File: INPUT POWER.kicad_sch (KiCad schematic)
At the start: 22 parts, among them J1 TYPE-C-31-M12_13, SW3 ON/OFF, U3 IP5306

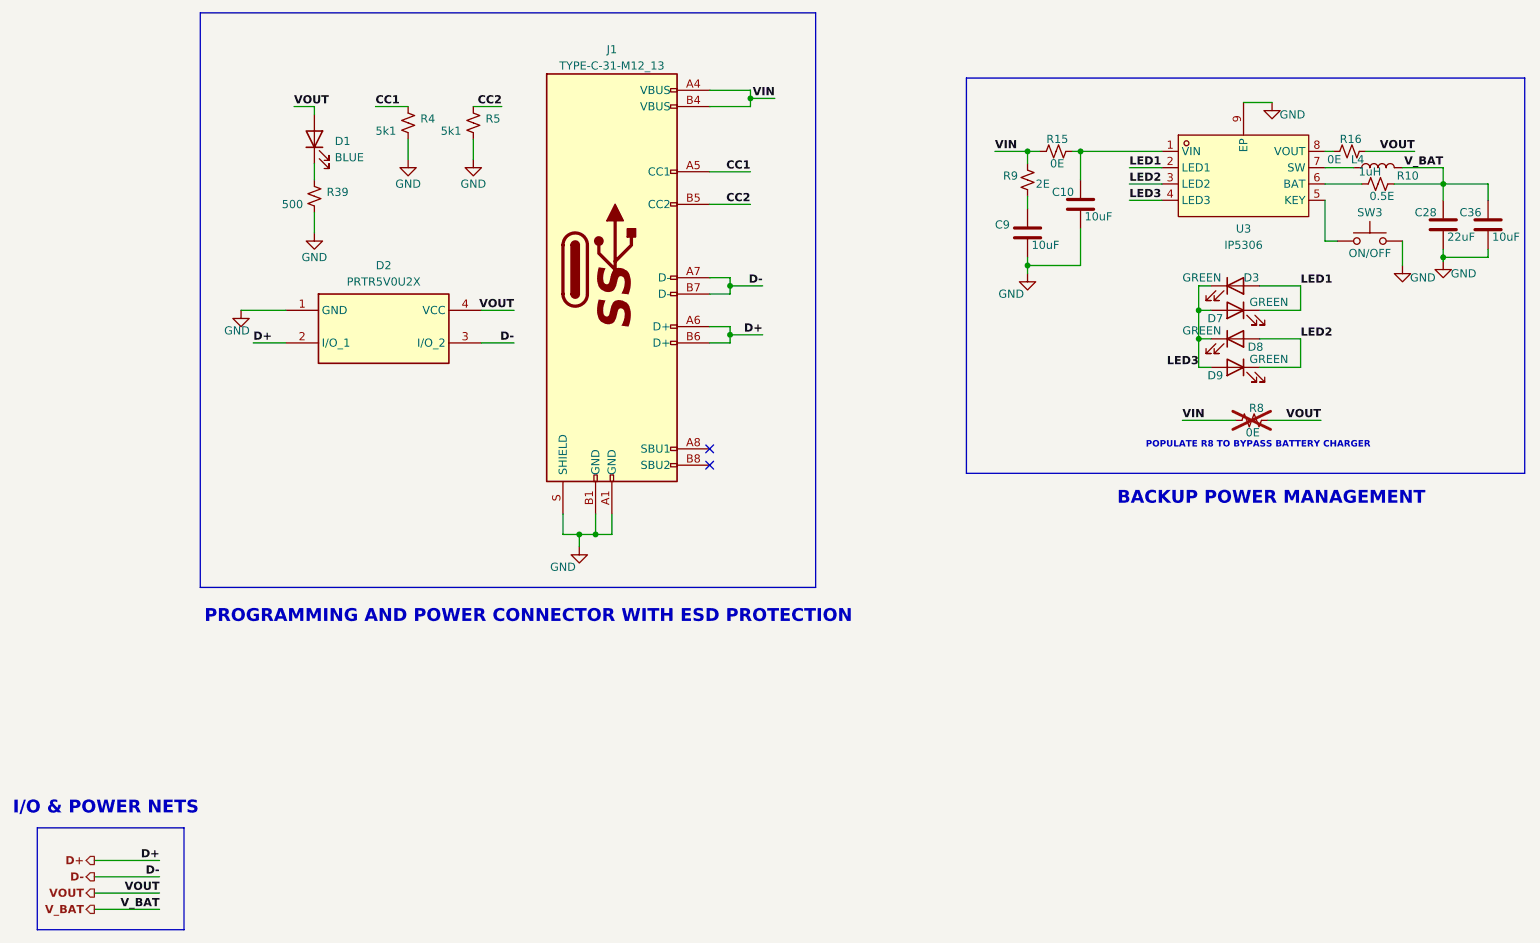
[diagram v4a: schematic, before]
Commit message: Added bulk Decoupling and arranged components
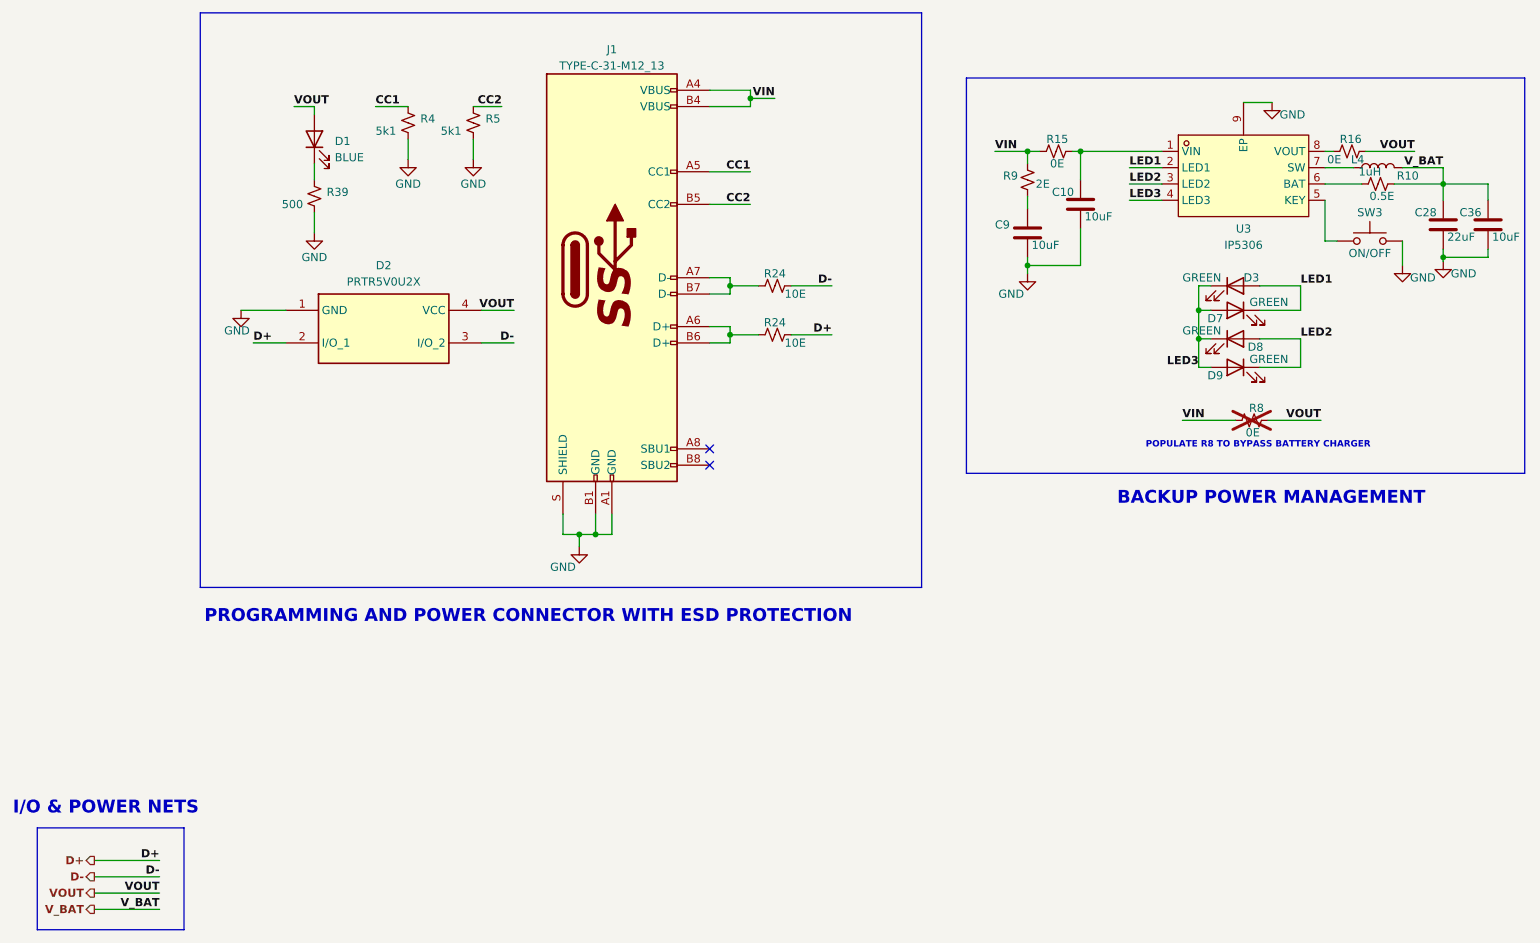
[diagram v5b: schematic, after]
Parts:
- added R24 (x2): 10E, ESP32-S3_Dev_Board:R_0402_1005Metric, symbol ESP32-S3_DB:R_Small_US
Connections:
- net D+: now also R24.2; no longer J1.A6 (D+), J1.B6 (D+)
- net D-: now also R24.2; no longer J1.A7 (D-), J1.B7 (D-)
- new net: J1.A7 (D-), J1.B7 (D-), R24.1
- new net: J1.A6 (D+), J1.B6 (D+), R24.1
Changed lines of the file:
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@@
     (stroke (width 1) (type default) (color 72 72 72 1))
   )
-  (bus (pts (xy 140.97 135.255) (xy 45.085 135.255))
+  (bus (pts (xy 157.48 135.255) (xy 45.085 135.255))
     (stroke (width 1) (type default) (color 72 72 72 1))
   )
@@
     (stroke (width 0) (type default))
   )
-  (wire (pts (xy 132.715 88.265) (xy 127.635 88.265))
+  (wire (pts (xy 143.51 88.265) (xy 137.16 88.265))
     (stroke (width 0) (type default))
   )
@@
     (stroke (width 0) (type default))
   )
-  (bus (pts (xy 45.085 45.72) (xy 140.97 45.72))
-    (stroke (width 1) (type default) (color 72 72 72 1))
-  )
-  (bus (pts (xy 140.97 45.72) (xy 140.97 135.255))
+  (bus (pts (xy 45.085 45.72) (xy 157.48 45.72))
+    (stroke (width 1) (type default) (color 72 72 72 1))
+  )
+  (bus (pts (xy 157.48 45.72) (xy 157.48 135.255))
     (stroke (width 1) (type default) (color 72 72 72 1))
   )
@@
     (stroke (width 0) (type default))
   )
+  (wire (pts (xy 132.08 95.885) (xy 127.635 95.885))
+    (stroke (width 0) (type default))
+  )
   (wire (pts (xy 231.14 72.39) (xy 238.76 72.39))
     (stroke (width 0) (type default))
@@
     (stroke (width 0) (type default))
   )
-  (wire (pts (xy 132.715 95.885) (xy 127.635 95.885))
+  (wire (pts (xy 143.51 95.885) (xy 137.16 95.885))
     (stroke (width 0) (type default))
   )
@@
   (bus (pts (xy 19.685 172.72) (xy 42.545 172.72))
     (stroke (width 1) (type default) (color 72 72 72 1))
+  )
+  (wire (pts (xy 132.08 88.265) (xy 127.635 88.265))
+    (stroke (width 0) (type default))
   )
   (wire (pts (xy 173.99 85.09) (xy 173.99 83.82))
@@
     (effects (font (size 1.27 1.27) (thickness 0.254) bold (color 255 153 0 1)) (justify left bottom))
   )
-  (label "D-" (at 132.715 88.265 180) (fields_autoplaced)
+  (label "D-" (at 143.51 88.265 180) (fields_autoplaced)
     (effects (font (size 1.27 1.27) (thickness 0.254) bold (color 0 0 255 1)) (justify right bottom))
   )
@@
     (effects (font (size 1.27 1.27) bold (color 132 132 0 1)) (justify right bottom))
   )
-  (label "D+" (at 132.715 95.885 180) (fields_autoplaced)
+  (label "D+" (at 143.51 95.885 180) (fields_autoplaced)
     (effects (font (size 1.27 1.27) (thickness 0.254) bold (color 0 0 255 1)) (justify right bottom))
   )
@@
         )
       )
+    )
+  )
+  (symbol (lib_id "ESP32-S3_DB:R_Small_US") (at 134.62 88.265 90) (unit 1)
+    (in_bom yes) (on_board yes) (dnp no)
+    (property "Reference" "R24" (at 134.62 86.36 90)
+      (effects (font (size 1.27 1.27)))
+    )
+    (property "Value" "10E" (at 137.795 89.535 90)
+      (effects (font (size 1.27 1.27)))
+    )
+    (property "Footprint" "ESP32-S3_Dev_Board:R_0402_1005Metric" (at 134.62 88.265 0)
+      (effects (font (size 1.27 1.27)) hide)
+    )
+    (property "Datasheet" "~" (at 134.62 88.265 0)
+      (effects (font (size 1.27 1.27)) hide)
+    )
+    (property "PN" "RTT02100JTH" (at 134.62 88.265 0)
+      (effects (font (size 1.27 1.27)) hide)
+    )
+    (pin "1")
+    (pin "2")
+    (instances
+      (project "ESP32-S3_DB"
+        (path "/b7fc4bd3-c219-4455-832b-8d795385dcf1/9b4afe2f-79e5-4a56-98d7-d16b193c0e70"
+          (reference "R24") (unit 1)
+        )
+        (path "/b7fc4bd3-c219-4455-832b-8d795385dcf1/95090a63-7b3c-4ea0-92b8-aeafe05264cd"
+          (reference "R47") (unit 1)
+        )
+      )
+    )
+  )
+  (symbol (lib_id "ESP32-S3_DB:R_Small_US") (at 134.62 95.885 90) (unit 1)
+    (in_bom yes) (on_board yes) (dnp no)
+    (property "Reference" "R24" (at 134.62 93.98 90)
+      (effects (font (size 1.27 1.27)))
+    )
+    (property "Value" "10E" (at 137.795 97.155 90)
+      (effects (font (size 1.27 1.27)))
+    )
+    (property "Footprint" "ESP32-S3_Dev_Board:R_0402_1005Metric" (at 134.62 95.885 0)
+      (effects (font (size 1.27 1.27)) hide)
+    )
+    (property "Datasheet" "~" (at 134.62 95.885 0)
+      (effects (font (size 1.27 1.27)) hide)
+    )
+    (property "PN" "RTT02100JTH" (at 134.62 95.885 0)
+      (effects (font (size 1.27 1.27)) hide)
+    )
+    (pin "1")
+    (pin "2")
+    (instances
+      (project "ESP32-S3_DB"
+        (path "/b7fc4bd3-c219-4455-832b-8d795385dcf1/9b4afe2f-79e5-4a56-98d7-d16b193c0e70"
+          (reference "R24") (unit 1)
+        )
+        (path "/b7fc4bd3-c219-4455-832b-8d795385dcf1/95090a63-7b3c-4ea0-92b8-aeafe05264cd"
+          (reference "R48") (unit 1)
+        )
+      )

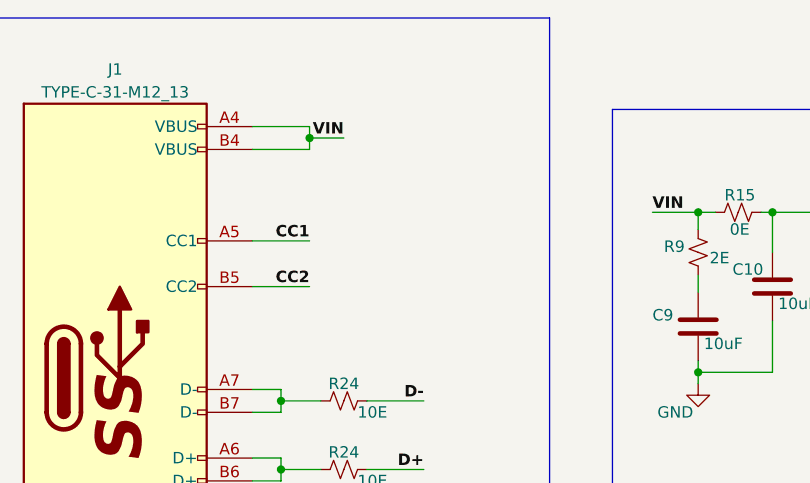
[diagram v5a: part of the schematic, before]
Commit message: Changed USB C footprint and arranged components
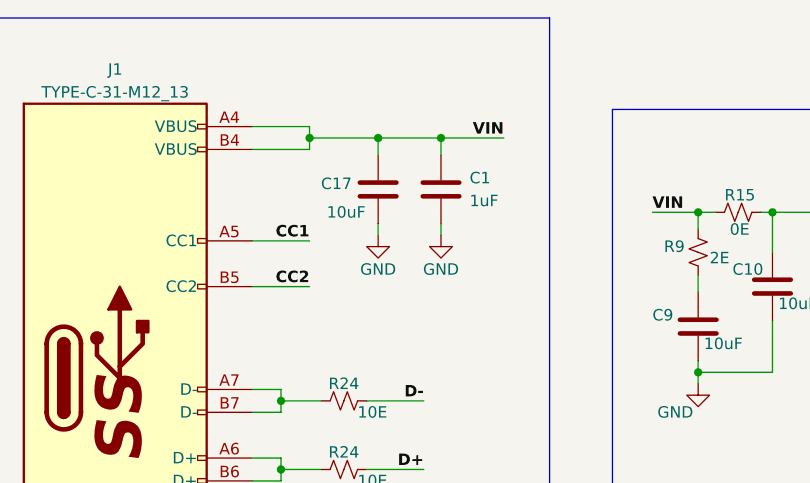
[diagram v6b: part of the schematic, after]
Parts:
- added C1: 1uF, ESP32-S3_Dev_Board:C_0603_1608Metric, symbol ESP32-S3_DB:C
- added C17: 10uF, ESP32-S3_Dev_Board:C_0805_2012Metric, symbol ESP32-S3_DB:C
- J1: footprint ESP32-S3_Dev_Board:USB-C_SMD-TYPE-C-31-M-12 -> ESP32-S3_Dev_Board:tyye_c_connector
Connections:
- net GND: now also C1.2, C17.2
- net VIN: now also C1.1, C17.1
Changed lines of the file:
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@@
 (kicad_sch (version 20230121) (generator eeschema)
   (paper "A4")
+  (junction (at 138.43 59.055) (diameter 0) (color 0 0 0 0)
+  )
   (junction (at 106.68 127) (diameter 0) (color 0 0 0 0)
   )
@@
   )
   (junction (at 238.76 83.82) (diameter 0) (color 0 0 0 0)
+  )
+  (junction (at 145.415 59.055) (diameter 0) (color 0 0 0 0)
   )
   (junction (at 130.81 59.055) (diameter 0) (color 0 0 0 0)
@@
     (stroke (width 0) (type default))
   )
+  (wire (pts (xy 145.415 60.96) (xy 145.415 59.055))
+    (stroke (width 0) (type default))
+  )
   (wire (pts (xy 238.76 69.85) (xy 232.41 69.85))
     (stroke (width 0) (type default))
@@
     (stroke (width 0.5) (type default) (color 132 132 0 1))
   )
-  (wire (pts (xy 134.62 59.055) (xy 130.81 59.055))
+  (wire (pts (xy 152.4 59.055) (xy 145.415 59.055))
     (stroke (width 0) (type default))
   )
@@
     (stroke (width 1) (type default) (color 72 72 72 1))
   )
+  (wire (pts (xy 138.43 69.85) (xy 138.43 68.58))
+    (stroke (width 0) (type default))
+  )
   (bus (pts (xy 157.48 45.72) (xy 157.48 135.255))
     (stroke (width 1) (type default) (color 72 72 72 1))
   )
+  (wire (pts (xy 145.415 69.85) (xy 145.415 68.58))
+    (stroke (width 0) (type default))
+  )
   (wire (pts (xy 130.81 70.485) (xy 124.46 70.485))
     (stroke (width 0) (type default))
@@
     (stroke (width 0) (type default))
   )
+  (wire (pts (xy 130.81 59.055) (xy 138.43 59.055))
+    (stroke (width 0) (type default))
+  )
   (wire (pts (xy 132.08 95.885) (xy 127.635 95.885))
     (stroke (width 0) (type default))
@@
   (bus (pts (xy 164.465 55.88) (xy 251.46 55.88))
     (stroke (width 1) (type default) (color 72 72 72 1))
+  )
+  (wire (pts (xy 138.43 60.96) (xy 138.43 59.055))
+    (stroke (width 0) (type default))
+  )
+  (wire (pts (xy 145.415 59.055) (xy 138.43 59.055))
+    (stroke (width 0) (type default))
   )
   (wire (pts (xy 62.865 71.755) (xy 62.865 69.215))
@@
     (effects (font (size 1.27 1.27) (thickness 0.254) bold (color 255 153 0 1)) (justify right bottom))
   )
-  (label "VIN" (at 134.62 59.055 180) (fields_autoplaced)
+  (label "VIN" (at 152.4 59.055 180) (fields_autoplaced)
     (effects (font (size 1.27 1.27) (thickness 0.254) bold (color 255 0 0 1)) (justify right bottom))
   )
@@
     (effects (font (size 1.27 1.27) (thickness 0.254) bold (color 0 0 255 1)) (justify right))
   )
+  (symbol (lib_id "ESP32-S3_DB:C") (at 145.415 64.77 0) (unit 1)
+    (in_bom yes) (on_board yes) (dnp no) (fields_autoplaced)
+    (property "Reference" "C1" (at 148.59 63.5 0)
+      (effects (font (size 1.27 1.27)) (justify left))
+    )
+    (property "Value" "1uF" (at 148.59 66.04 0)
+      (effects (font (size 1.27 1.27)) (justify left))
+    )
+    (property "Footprint" "ESP32-S3_Dev_Board:C_0603_1608Metric" (at 146.3802 68.58 0)
+      (effects (font (size 1.27 1.27)) hide)
+    )
+    (property "Datasheet" "~" (at 145.415 64.77 0)
+      (effects (font (size 1.27 1.27)) hide)
+    )
+    (property "PN" "CC0603KRX5R8BB105" (at 145.415 64.77 0)
+      (effects (font (size 1.27 1.27)) hide)
+    )
+    (pin "1")
+    (pin "2")
+    (instances
+      (project "ESP32-S3_DB"
+        (path "/b7fc4bd3-c219-4455-832b-8d795385dcf1/efdd6c4f-0b42-4473-ae3b-b7dbb76b2e75"
+          (reference "C1") (unit 1)
+        )
+        (path "/b7fc4bd3-c219-4455-832b-8d795385dcf1/95090a63-7b3c-4ea0-92b8-aeafe05264cd"
+          (reference "C41") (unit 1)
+        )
+      )
+    )
+  )
   (symbol (lib_id "ESP32-S3_DB:R_Small_US") (at 224.155 67.31 90) (unit 1)
     (in_bom yes) (on_board yes) (dnp no)
@@
         (path "/b7fc4bd3-c219-4455-832b-8d795385dcf1/95090a63-7b3c-4ea0-92b8-aeafe05264cd"
           (reference "R16") (unit 1)
+        )
+      )
+    )
+  )
+  (symbol (lib_id "ESP32-S3_DB:GND") (at 138.43 69.85 0) (unit 1)
+    (in_bom yes) (on_board yes) (dnp no)
+    (property "Reference" "#PWR067" (at 138.43 76.2 0)
+      (effects (font (size 1.27 1.27)) hide)
+    )
+    (property "Value" "GND" (at 138.43 73.66 0)
+      (effects (font (size 1.27 1.27)))
+    )
+    (property "Footprint" "" (at 138.43 69.85 0)
+      (effects (font (size 1.27 1.27)) hide)
+    )
+    (property "Datasheet" "" (at 138.43 69.85 0)
+      (effects (font (size 1.27 1.27)) hide)
+    )
+    (pin "1")
+    (instances
+      (project "ESP32-S3_DB"
+        (path "/b7fc4bd3-c219-4455-832b-8d795385dcf1/95090a63-7b3c-4ea0-92b8-aeafe05264cd"
+          (reference "#PWR067") (unit 1)
         )
       )
@@
         (path "/b7fc4bd3-c219-4455-832b-8d795385dcf1/95090a63-7b3c-4ea0-92b8-aeafe05264cd"
           (reference "#PWR053") (unit 1)
+        )
+      )
+    )
+  )
+  (symbol (lib_id "ESP32-S3_DB:C") (at 138.43 64.77 0) (unit 1)
+    (in_bom yes) (on_board yes) (dnp no)
+    (property "Reference" "C17" (at 132.08 64.135 0)
+      (effects (font (size 1.27 1.27)) (justify left))
+    )
+    (property "Value" "10uF" (at 132.715 67.31 0)
+      (effects (font (size 1.27 1.27)) (justify left))
+    )
+    (property "Footprint" "ESP32-S3_Dev_Board:C_0805_2012Metric" (at 139.3952 68.58 0)
+      (effects (font (size 1.27 1.27)) hide)
+    )
+    (property "Datasheet" "~" (at 138.43 64.77 0)
+      (effects (font (size 1.27 1.27)) hide)
+    )
+    (property "PN" "CL21A106KAYNNNE" (at 138.43 64.77 0)
+      (effects (font (size 1.27 1.27)) hide)
+    )
+    (pin "1")
+    (pin "2")
+    (instances
+      (project "ESP32-S3_DB"
+        (path "/b7fc4bd3-c219-4455-832b-8d795385dcf1/efdd6c4f-0b42-4473-ae3b-b7dbb76b2e75"
+          (reference "C17") (unit 1)
+        )
+        (path "/b7fc4bd3-c219-4455-832b-8d795385dcf1/95090a63-7b3c-4ea0-92b8-aeafe05264cd"
+          (reference "C40") (unit 1)
         )
       )
@@
       (effects (font (size 1.27 1.27)))
     )
-    (property "Footprint" "ESP32-S3_Dev_Board:USB-C_SMD-TYPE-C-31-M-12" (at 96.52 85.725 90)
+    (property "Footprint" "ESP32-S3_Dev_Board:tyye_c_connector" (at 96.52 85.725 90)
       (effects (font (size 1.27 1.27)) hide)
     )
@@
         )
       )
+    )
+  )
+  (symbol (lib_id "ESP32-S3_DB:GND") (at 145.415 69.85 0) (unit 1)
+    (in_bom yes) (on_board yes) (dnp no)
+    (property "Reference" "#PWR068" (at 145.415 76.2 0)
+      (effects (font (size 1.27 1.27)) hide)
+    )
+    (property "Value" "GND" (at 145.415 73.66 0)
+      (effects (font (size 1.27 1.27)))
+    )
+    (property "Footprint" "" (at 145.415 69.85 0)
+      (effects (font (size 1.27 1.27)) hide)
+    )
+    (property "Datasheet" "" (at 145.415 69.85 0)
+      (effects (font (size 1.27 1.27)) hide)
+    )
+    (pin "1")
+    (instances
+      (project "ESP32-S3_DB"
+        (path "/b7fc4bd3-c219-4455-832b-8d795385dcf1/95090a63-7b3c-4ea0-92b8-aeafe05264cd"
+          (reference "#PWR068") (unit 1)
+        )
+      )
